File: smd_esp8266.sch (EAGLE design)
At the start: 21 parts, among them IC1 LM1117S, IC2 DS3231/SO, U1 ESP8266-12E/ESP-12E

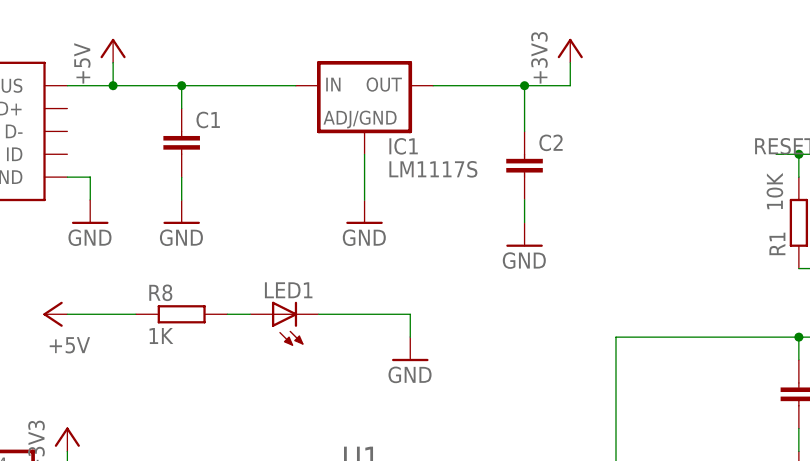
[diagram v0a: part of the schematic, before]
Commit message: updated decoupling capacitor values
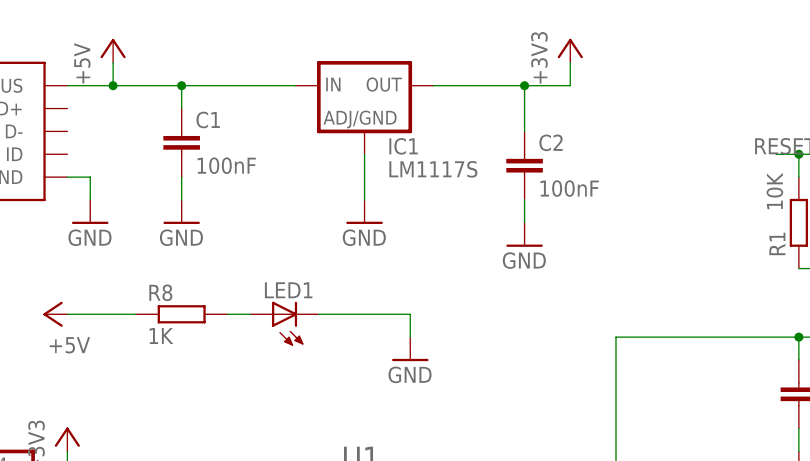
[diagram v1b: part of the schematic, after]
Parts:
- C1, C2: value (none) -> 100nF
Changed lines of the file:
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@@
 <part name="IC1" library="LM1117" deviceset="LM1117" device="S"/>
 <part name="CN1" library="adafruit" library_urn="urn:adsk.eagle:library:420" deviceset="USB" device="MINIB" package3d_urn="urn:adsk.eagle:package:6240633/1"/>
-<part name="C1" library="rcl" library_urn="urn:adsk.eagle:library:334" deviceset="C-EU" device="C0805" package3d_urn="urn:adsk.eagle:package:23617/2"/>
-<part name="C2" library="rcl" library_urn="urn:adsk.eagle:library:334" deviceset="C-EU" device="C0805" package3d_urn="urn:adsk.eagle:package:23617/2"/>
+<part name="C1" library="rcl" library_urn="urn:adsk.eagle:library:334" deviceset="C-EU" device="C0805" package3d_urn="urn:adsk.eagle:package:23617/2" value="100nF"/>
+<part name="C2" library="rcl" library_urn="urn:adsk.eagle:library:334" deviceset="C-EU" device="C0805" package3d_urn="urn:adsk.eagle:package:23617/2" value="100nF"/>
 <part name="C3" library="rcl" library_urn="urn:adsk.eagle:library:334" deviceset="C-EU" device="C0805" package3d_urn="urn:adsk.eagle:package:23617/2"/>
 <part name="C4" library="rcl" library_urn="urn:adsk.eagle:library:334" deviceset="C-EU" device="C0805" package3d_urn="urn:adsk.eagle:package:23617/2"/>
